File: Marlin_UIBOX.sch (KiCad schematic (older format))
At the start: 9 parts, among them J1 EXP1, J2 EXP2, J3 12864OLED_SPI, J4 SD_CARD, J5 ROT_ENCODER, Q1 2N3904

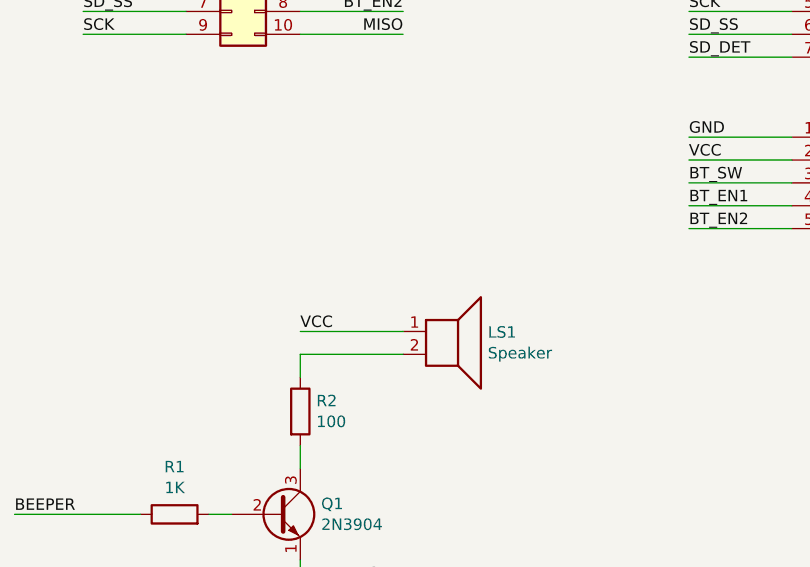
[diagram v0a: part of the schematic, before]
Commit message: PCB ver2 full board to board connections
* Complete re-do PCB to have PCB to PCB connectors no wire needed
* Went with 2 layer PCB instead of trying to make single layer...
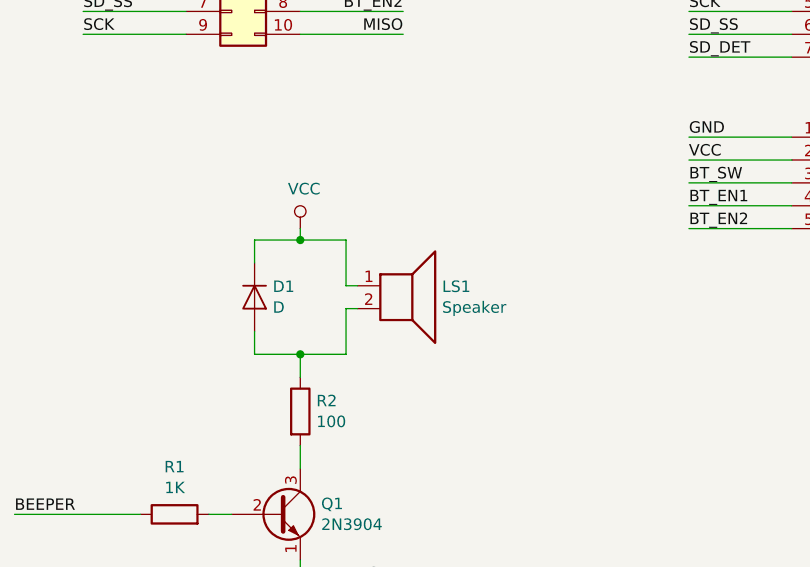
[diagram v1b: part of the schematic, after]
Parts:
- added D1: D, Diode_THT:D_DO-35_SOD27_P7.62mm_Horizontal, symbol Device:D
- J3: footprint Pin_Headers:Pin_Header_Straight_1x07_Pitch2.54mm -> Connector_PinSocket_2.54mm:PinSocket_1x07_P2.54mm_Vertical
- J5: footprint Pin_Headers:Pin_Header_Straight_1x05_Pitch2.54mm -> Connector_PinSocket_2.54mm:PinSocket_1x05_P2.54mm_Vertical
- LS1: footprint Buzzers_Beepers:Buzzer_12x9.5RM7.6 -> Buzzer_Beeper:Buzzer_12x9.5RM7.6
- Q1: footprint TO_SOT_Packages_THT:TO-92_Inline_Narrow_Oval -> Package_TO_SOT_THT:TO-92_Inline
- R1, R2: footprint Resistors_ThroughHole:R_Axial_DIN0207_L6.3mm_D2.5mm_P7.62mm_Horizontal -> Resistor_THT:R_Axial_DIN0207_L6.3mm_D2.5mm_P7.62mm_Horizontal
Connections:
- net VCC: now also D1.1 (K)
- net at LS1.2, R2.1: now also D1.2 (A)
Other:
- moved on the sheet: LS1
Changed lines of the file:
@@
 EESchema Schematic File Version 4
+LIBS:Marlin_UIBOX-cache
 EELAYER 26 0
 EELAYER END
@@
 F 0 "J3" H 4979 2042 50  0000 L CNN
 F 1 "12864OLED_SPI" H 4979 1951 50  0000 L CNN
-F 2 "Pin_Headers:Pin_Header_Straight_1x07_Pitch2.54mm" H 4900 2000 50  0001 C CNN
+F 2 "Connector_PinSocket_2.54mm:PinSocket_1x07_P2.54mm_Vertical" H 4900 2000 50  0001 C CNN
 F 3 "~" H 4900 2000 50  0001 C CNN
 	1    4900 2000
@@
 F 0 "J5" H 4979 3842 50  0000 L CNN
 F 1 "ROT_ENCODER" H 4979 3751 50  0000 L CNN
-F 2 "Pin_Headers:Pin_Header_Straight_1x05_Pitch2.54mm" H 4900 3800 50  0001 C CNN
+F 2 "Connector_PinSocket_2.54mm:PinSocket_1x05_P2.54mm_Vertical" H 4900 3800 50  0001 C CNN
 F 3 "~" H 4900 3800 50  0001 C CNN
 	1    4900 3800
@@
 L Device:Speaker LS1
 U 1 1 5C1DB791
-P 3200 4450
-F 0 "LS1" H 3370 4446 50  0000 L CNN
-F 1 "Speaker" H 3370 4355 50  0000 L CNN
-F 2 "Buzzers_Beepers:Buzzer_12x9.5RM7.6" H 3200 4250 50  0001 C CNN
-F 3 "~" H 3190 4400 50  0001 C CNN
-	1    3200 4450
+P 3000 4250
+F 0 "LS1" H 3170 4246 50  0000 L CNN
+F 1 "Speaker" H 3170 4155 50  0000 L CNN
+F 2 "Buzzer_Beeper:Buzzer_12x9.5RM7.6" H 3000 4050 50  0001 C CNN
+F 3 "~" H 2990 4200 50  0001 C CNN
+	1    3000 4250
 	1    0    0    -1
 $EndComp
@@
 F 0 "R2" H 2620 4846 50  0000 L CNN
 F 1 "100" H 2620 4755 50  0000 L CNN
-F 2 "Resistors_ThroughHole:R_Axial_DIN0207_L6.3mm_D2.5mm_P7.62mm_Horizontal" V 2480 4800 50  0001 C CNN
+F 2 "Resistor_THT:R_Axial_DIN0207_L6.3mm_D2.5mm_P7.62mm_Horizontal" V 2480 4800 50  0001 C CNN
 F 3 "~" H 2550 4800 50  0001 C CNN
 	1    2550 4800
@@
 F 0 "R1" V 2207 5250 50  0000 C CNN
 F 1 "1K" V 2116 5250 50  0000 C CNN
-F 2 "Resistors_ThroughHole:R_Axial_DIN0207_L6.3mm_D2.5mm_P7.62mm_Horizontal" V 1930 5250 50  0001 C CNN
+F 2 "Resistor_THT:R_Axial_DIN0207_L6.3mm_D2.5mm_P7.62mm_Horizontal" V 1930 5250 50  0001 C CNN
 F 3 "~" H 2000 5250 50  0001 C CNN
 	1    2000 5250
@@
 F 0 "Q1" H 2641 5296 50  0000 L CNN
 F 1 "2N3904" H 2641 5205 50  0000 L CNN
-F 2 "TO_SOT_Packages_THT:TO-92_Inline_Narrow_Oval" H 2650 5175 50  0001 L CIN
+F 2 "Package_TO_SOT_THT:TO-92_Inline" H 2650 5175 50  0001 L CIN
 F 3 "https://www.fairchildsemi.com/datasheets/2N/2N3904.pdf" H 2450 5250 50  0001 L CNN
 	1    2450 5250
@@
 BT_EN2
 Wire Wire Line
-	3000 4450 2550 4450
-Wire Wire Line
-	3000 4550 2550 4550
-Text Label 2550 4450 0    50   ~ 0
-VCC
-Wire Wire Line
 	2550 4550 2550 4650
 Wire Wire Line
@@
 Wire Wire Line
 	2550 4950 2550 5050
+Wire Wire Line
+	2350 4550 2550 4550
+Wire Wire Line
+	2750 4550 2750 4350
+Wire Wire Line
+	2750 4350 2800 4350
+Wire Wire Line
+	2750 4250 2750 4050
+Wire Wire Line
+	2750 4050 2550 4050
+Wire Wire Line
+	2750 4250 2800 4250
+Connection ~ 2550 4550
+Wire Wire Line
+	2550 4550 2750 4550
+$Comp
+L power:VCC #PWR03
+U 1 1 5C309C0B
+P 2550 4000
+F 0 "#PWR03" H 2550 3850 50  0001 C CNN
+F 1 "VCC" H 2567 4173 50  0000 C CNN
+F 2 "" H 2550 4000 50  0001 C CNN
+F 3 "" H 2550 4000 50  0001 C CNN
+	1    2550 4000
+	1    0    0    -1
+$EndComp
+Wire Wire Line
+	2550 4000 2550 4050
+Connection ~ 2550 4050
+Wire Wire Line
+	2550 4050 2350 4050
+$Comp
+L Device:D D1
+U 1 1 5C30C238
+P 2350 4300
+F 0 "D1" V 2304 4379 50  0000 L CNN
+F 1 "D" V 2395 4379 50  0000 L CNN
+F 2 "Diode_THT:D_DO-35_SOD27_P7.62mm_Horizontal" H 2350 4300 50  0001 C CNN
+F 3 "~" H 2350 4300 50  0001 C CNN
+	1    2350 4300
+	0    1    1    0
+$EndComp
+Wire Wire Line
+	2350 4450 2350 4550
+Wire Wire Line
+	2350 4050 2350 4150
 $EndSCHEMATC

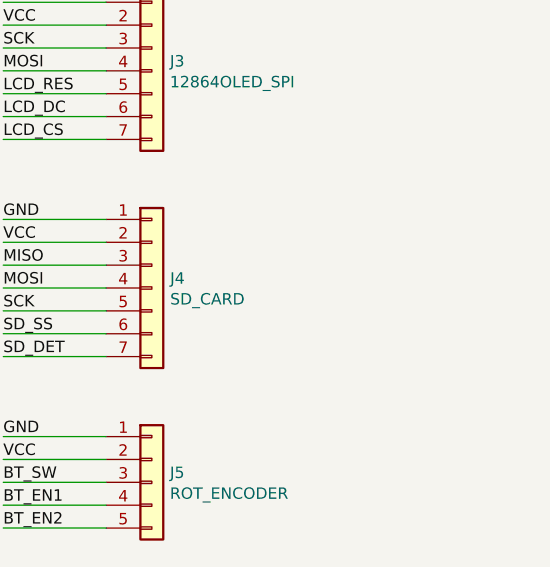
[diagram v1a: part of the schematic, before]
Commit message: Added second header for second position on SD card pcb
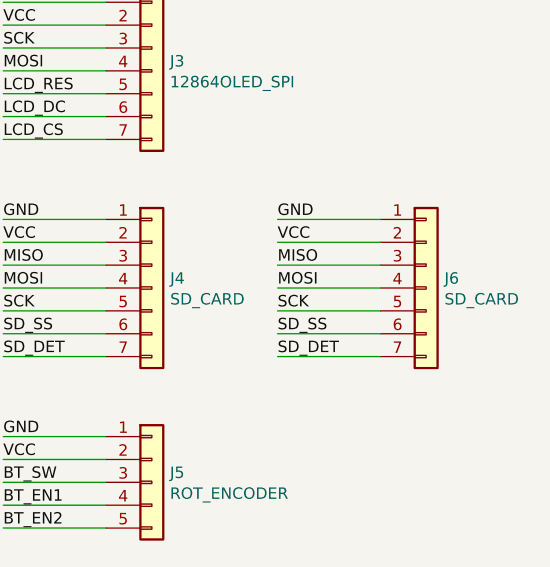
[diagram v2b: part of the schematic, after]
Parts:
- added J6: SD_CARD, Pin_Headers:Pin_Header_Straight_1x07_Pitch2.54mm, symbol Connector_Generic:Conn_01x07
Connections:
- net GND: now also J6.1 (Pin_1)
- net MISO: now also J6.3 (Pin_3)
- net MOSI: now also J6.4 (Pin_4)
- net SCK: now also J6.5 (Pin_5)
- net SD_DET: now also J6.7 (Pin_7)
- net SD_SS: now also J6.6 (Pin_6)
- net VCC: now also J6.2 (Pin_2)
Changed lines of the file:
@@
 EESchema Schematic File Version 4
-LIBS:Marlin_UIBOX-cache
-EELAYER 26 0
+EELAYER 30 0
 EELAYER END
 $Descr A4 11693 8268
@@
 Wire Wire Line
 	2350 4050 2350 4150
+$Comp
+L Connector_Generic:Conn_01x07 J6
+U 1 1 5E46BFFF
+P 6100 2950
+F 0 "J6" H 6180 2992 50  0000 L CNN
+F 1 "SD_CARD" H 6180 2901 50  0000 L CNN
+F 2 "Pin_Headers:Pin_Header_Straight_1x07_Pitch2.54mm" H 6100 2950 50  0001 C CNN
+F 3 "~" H 6100 2950 50  0001 C CNN
+	1    6100 2950
+	1    0    0    -1
+$EndComp
+Wire Wire Line
+	5900 2750 5450 2750
+Text Label 5450 3050 0    50   ~ 0
+SCK
+Text Label 5450 2950 0    50   ~ 0
+MOSI
+Text Label 5450 2650 0    50   ~ 0
+GND
+Text Label 5450 2750 0    50   ~ 0
+VCC
+Text Label 5450 2850 0    50   ~ 0
+MISO
+Text Label 5450 3150 0    50   ~ 0
+SD_SS
+Text Label 5450 3250 0    50   ~ 0
+SD_DET
+Wire Wire Line
+	5900 2650 5450 2650
+Wire Wire Line
+	5900 2850 5450 2850
+Wire Wire Line
+	5900 2950 5450 2950
+Wire Wire Line
+	5900 3050 5450 3050
+Wire Wire Line
+	5900 3150 5450 3150
+Wire Wire Line
+	5900 3250 5450 3250
 $EndSCHEMATC

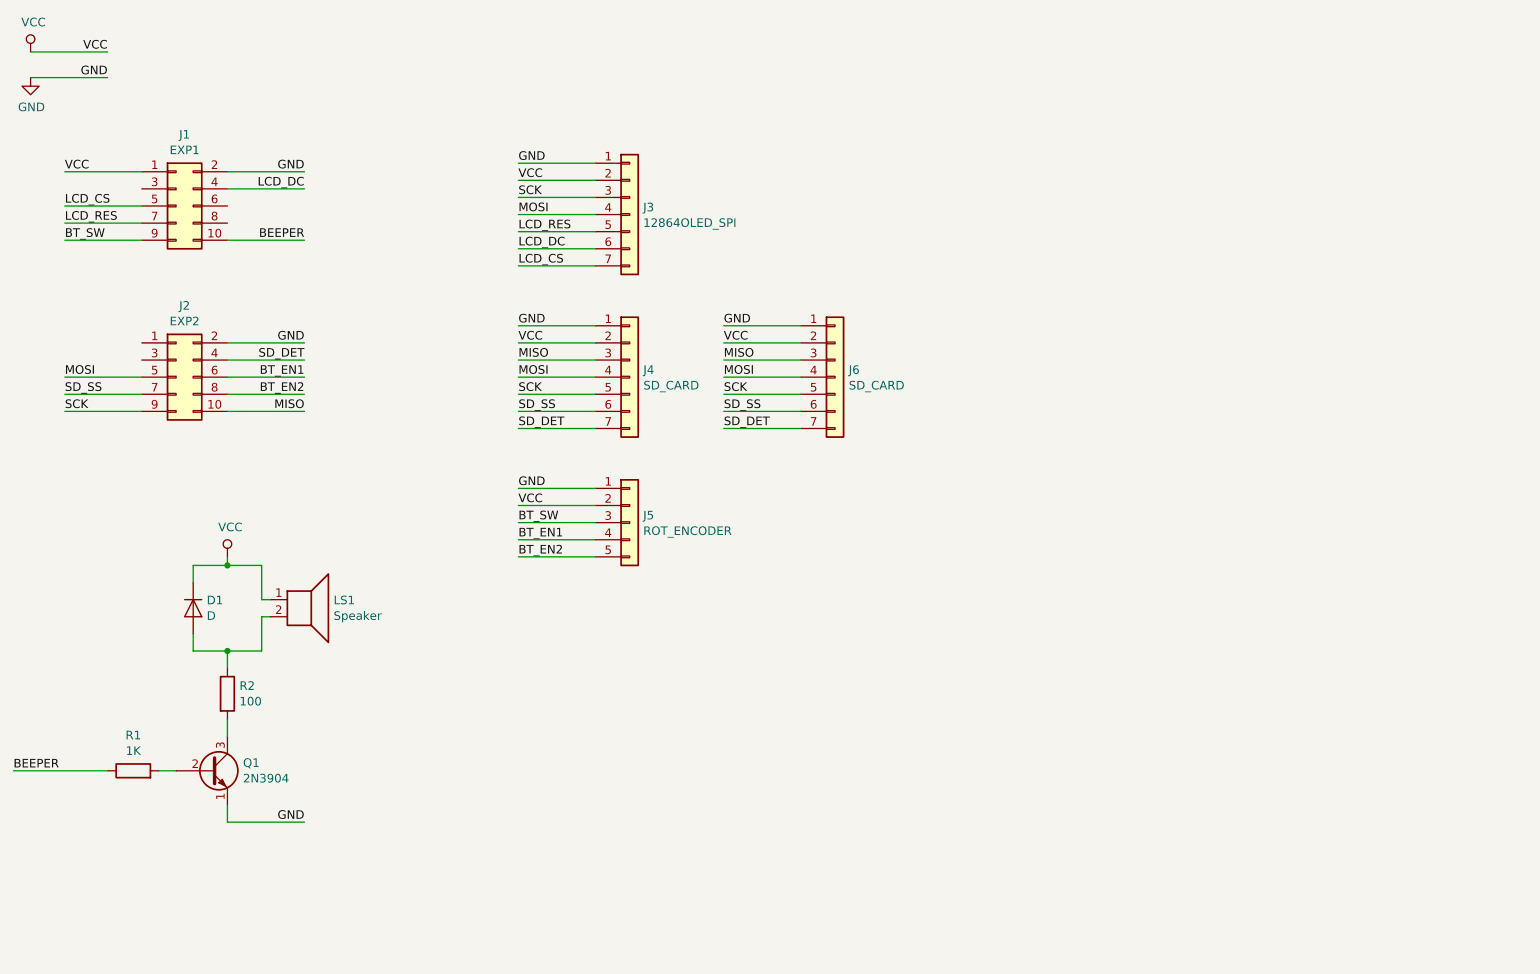
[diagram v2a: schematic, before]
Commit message: Added 3.3V Reg for LCD
* Added 3.3V Reg for LCD
* Added optional pull up resistors for LCD
* Added series resistors fro SPI signal for LCD to help with over/under
shoot
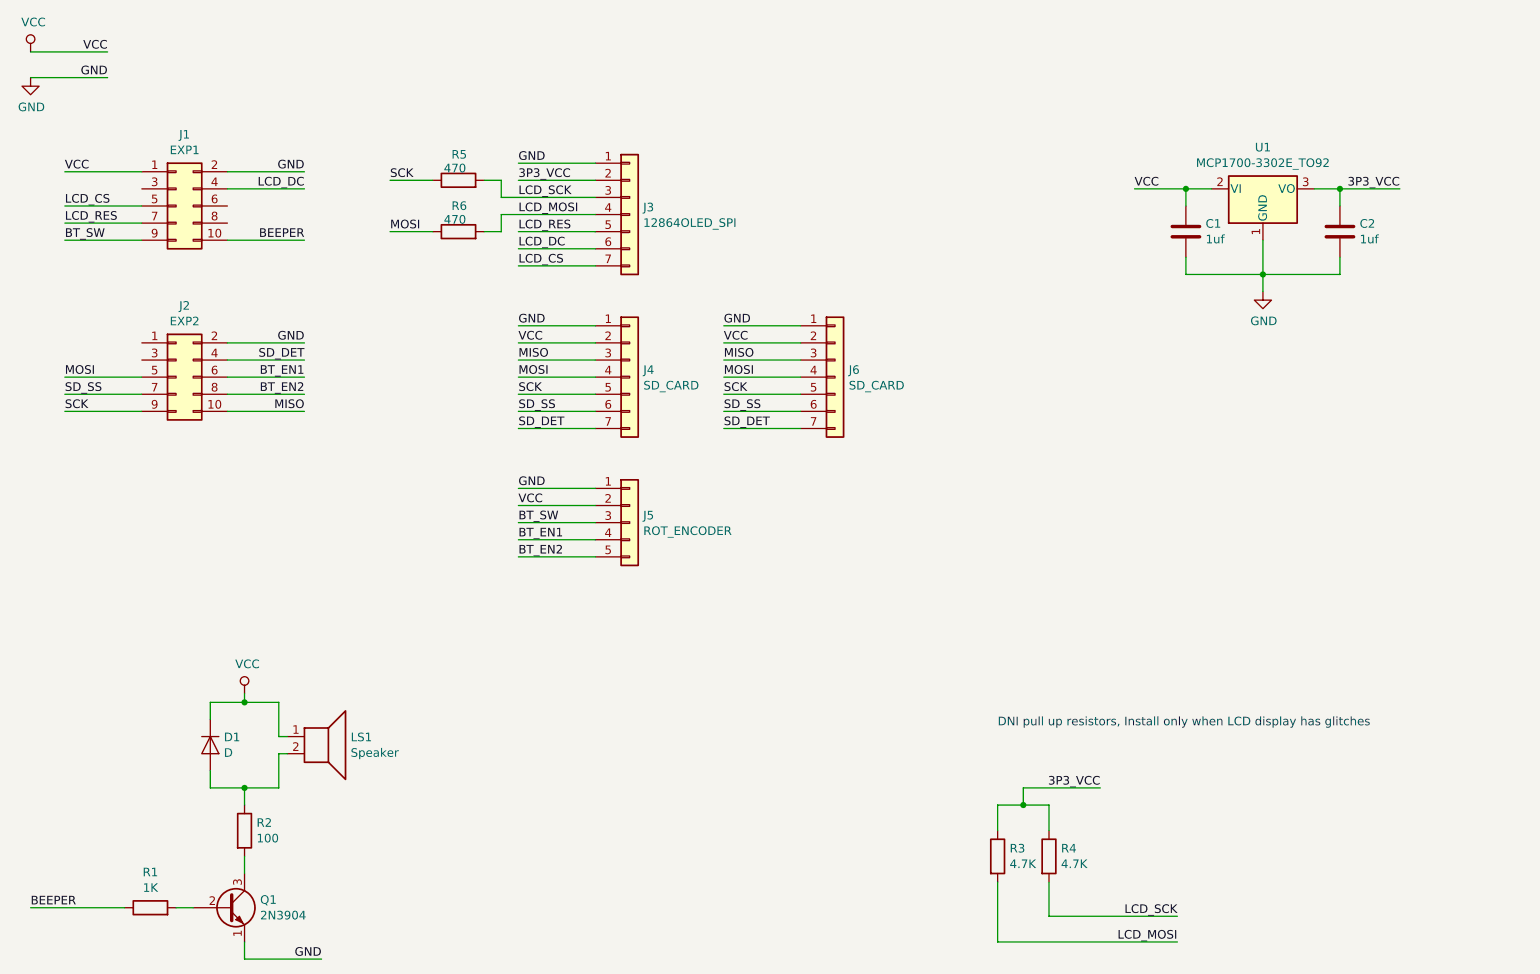
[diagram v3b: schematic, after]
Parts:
- added C1, C2: 1uf, Capacitor_THT:C_Rect_L4.6mm_W2.0mm_P2.50mm_MKS02_FKP02, symbol Device:C
- added R3, R4: 4.7K, Resistor_THT:R_Axial_DIN0207_L6.3mm_D2.5mm_P7.62mm_Horizontal, symbol Device:R
- added R5, R6: 470, Resistor_THT:R_Axial_DIN0207_L6.3mm_D2.5mm_P7.62mm_Horizontal, symbol Device:R
- added U1: MCP1700-3302E_TO92, Package_TO_SOT_THT:TO-92_Inline, symbol Regulator_Linear:MCP1700-3302E_TO92
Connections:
- net GND: now also C1.2, C2.2, U1.1 (GND)
- net MOSI: now also R6.1; no longer J3.4 (Pin_4)
- net SCK: now also R5.1; no longer J3.3 (Pin_3)
- net VCC: now also C1.1, U1.2 (VI); no longer J3.2 (Pin_2)
- new net 3P3_VCC: C2.1, J3.2 (Pin_2), R3.1, R4.1, U1.3 (VO)
- new net LCD_MOSI: J3.4 (Pin_4), R3.2, R6.2
- new net LCD_SCK: J3.3 (Pin_3), R4.2, R5.2
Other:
- note added: "DNI pull up resistors, Install only when LCD display has glitches"
- moved on the sheet: D1, LS1, Q1, R1, R2
